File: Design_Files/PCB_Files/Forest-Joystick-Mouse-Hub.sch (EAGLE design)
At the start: 24 parts, among them J1 E5566-Q0LK22-L

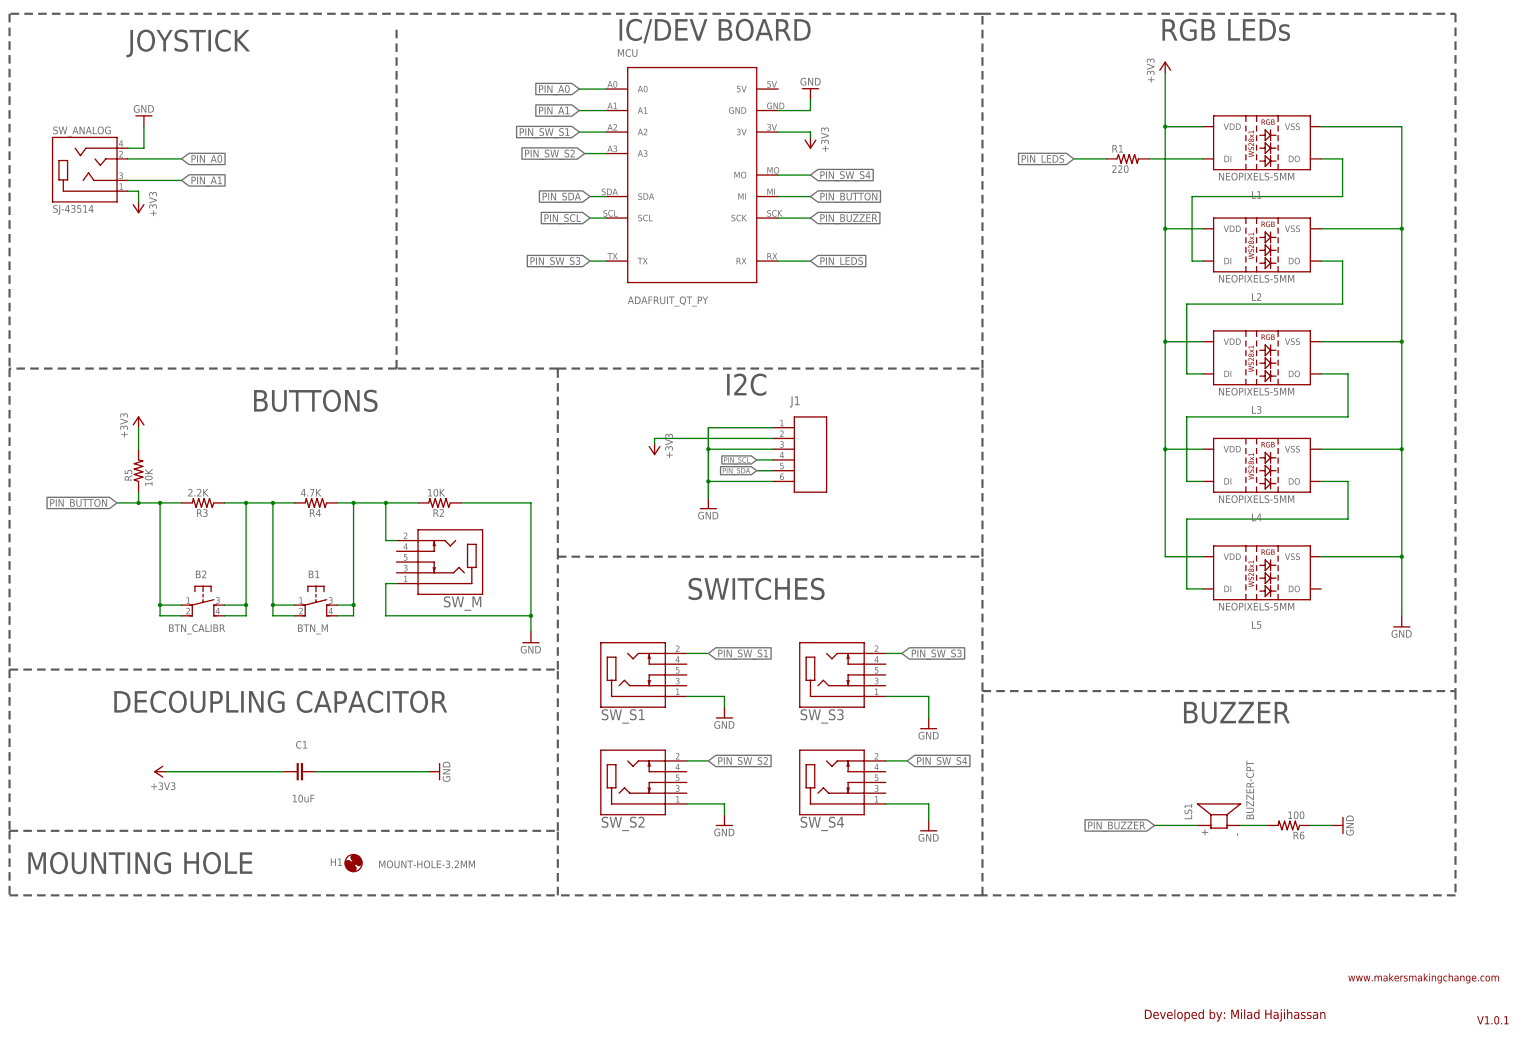
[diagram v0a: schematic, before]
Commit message: PCB Updates
 - Footprint for larger resistors
 - Added OSHWA Certification logo
 - Updated Gerbers
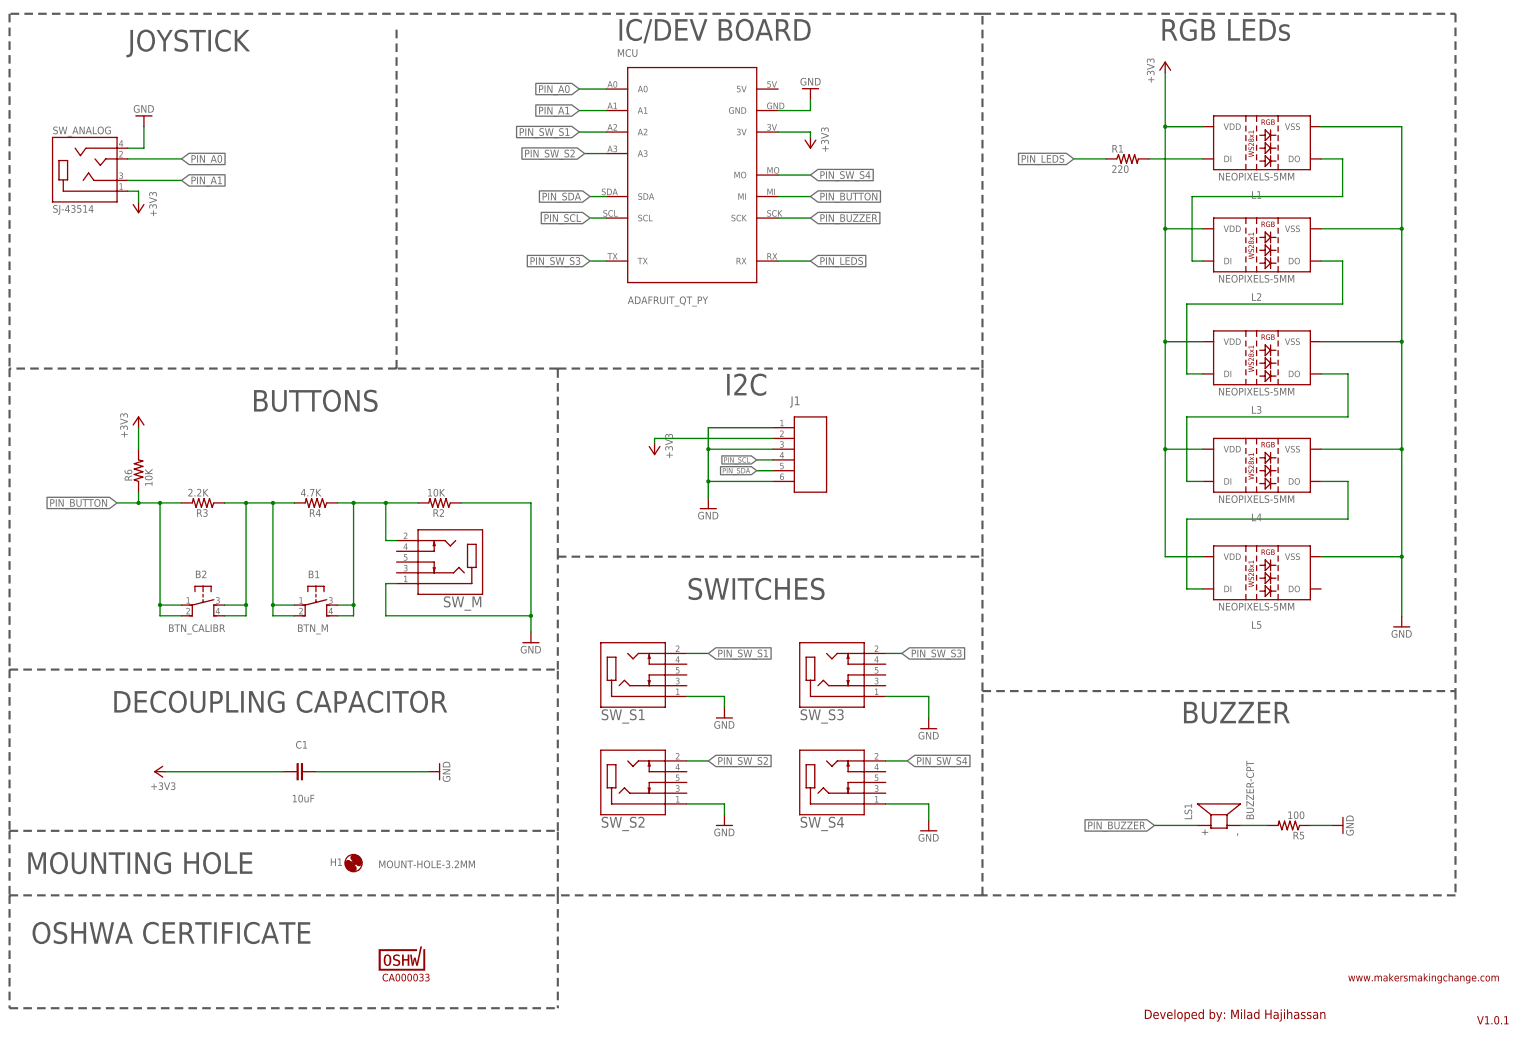
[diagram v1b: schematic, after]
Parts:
- added LOGO-OSHWA: CA000033, MMC Eagle:OSHWA-LOGO-SMALL
- R5: value 10K -> 100
- R6: value 100 -> 10K
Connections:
- net +3V3: now also R6.2; no longer R5.2
- net GND: now also R5.1; no longer R6.1
- net N$12: now also R5.2; no longer R6.2
- net PIN_BUTTON: now also R6.1; no longer R5.1
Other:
- note added: "OSHWA CERTIFICATE"
- moved on the sheet: R5, R6
